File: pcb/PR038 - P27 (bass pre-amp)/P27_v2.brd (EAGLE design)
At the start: 45.1 x 52.1 mm, 52 parts, among them IC1 NE5532U, IC2 LM317, IC3 LM337, T1 BC549

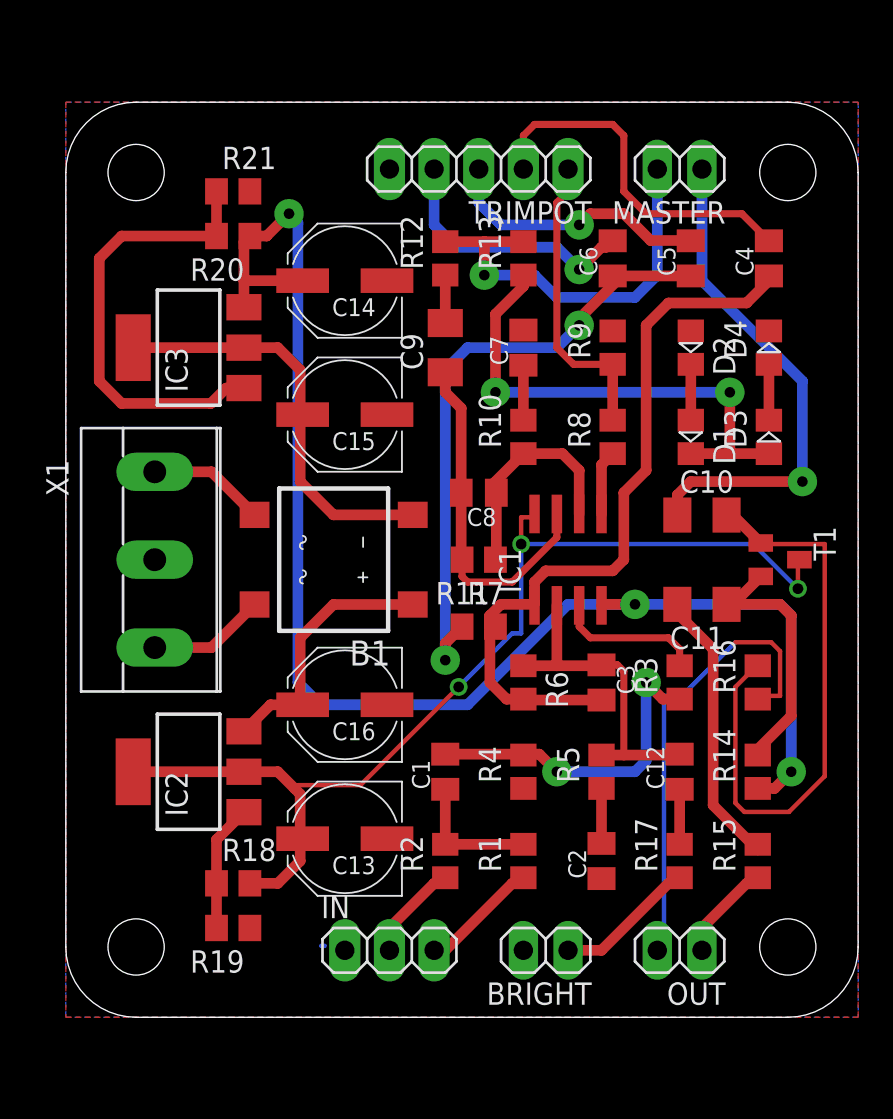
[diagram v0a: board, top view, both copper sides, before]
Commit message: 
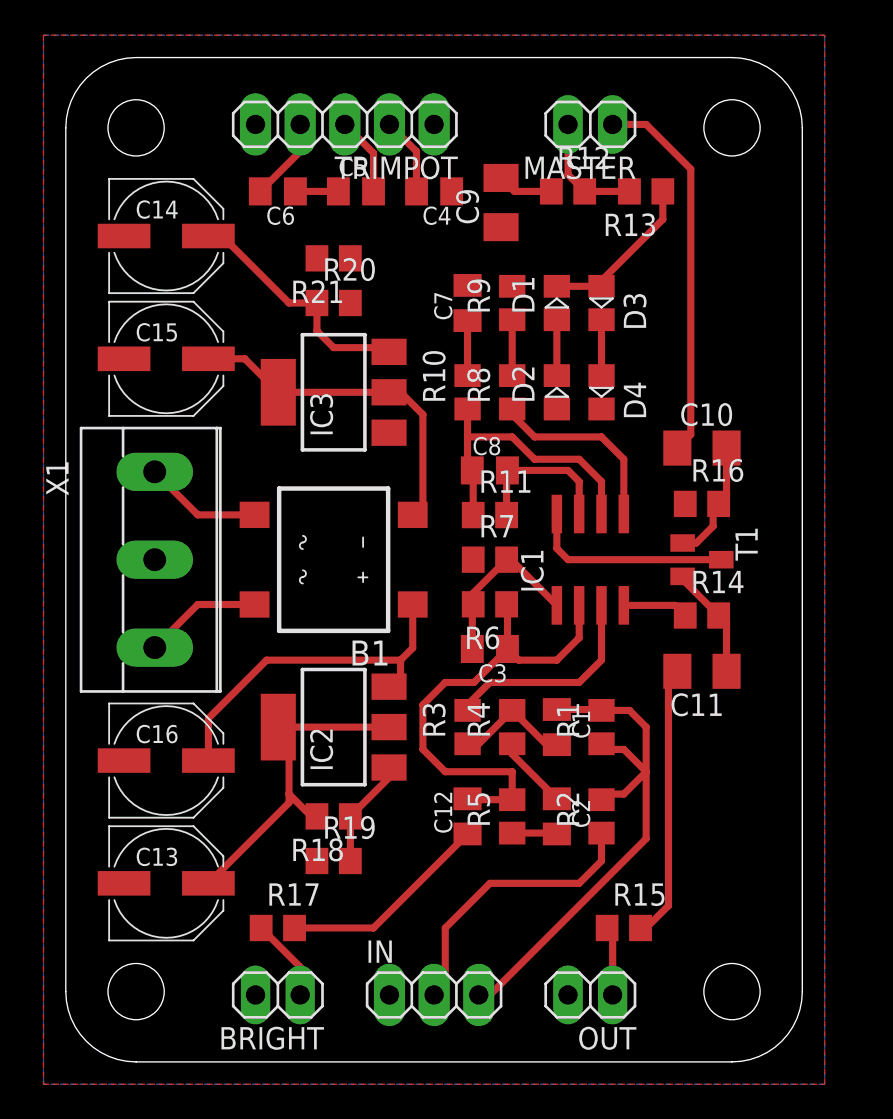
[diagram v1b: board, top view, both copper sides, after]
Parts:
- moved R17 23.2 mm to (12.1, 5.08), turned to 0 degrees
- moved C4 19.4 mm to (21.0, 47.0), turned to 180 degrees
- moved C5 19.4 mm to (16.5, 47.0), turned to 0 degrees
- moved C6 19.4 mm to (12.1, 47.0), turned to 180 degrees
- moved BRIGHT 15.5 mm to (12.1, 1.27)
- moved C12 12.3 mm to (22.9, 11.4)
- moved R3 12.3 mm to (22.9, 16.5)
- moved D3 12.2 mm to (30.5, 40.6), turned to 270 degrees
- moved D1 10.8 mm to (27.9, 40.6), turned to 90 degrees
- moved C15 10.6 mm to (5.71, 37.5), turned to 0 degrees
- moved C16 10.6 mm to (5.71, 14.6), turned to 0 degrees
- moved R16 10.6 mm to (36.2, 29.2), turned to 0 degrees
- moved C13 10.5 mm to (5.71, 7.62), turned to 0 degrees
- moved C14 10.5 mm to (5.71, 44.5), turned to 0 degrees
- moved D4 9.86 mm to (30.5, 35.6), turned to 270 degrees
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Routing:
- net -12V: track 81.8 -> 17.7 mm, vias 3 -> 0
- net N$8: track 36.5 -> 2.45 mm, vias 2 -> 0
- net N$6: track 42.9 -> 9.82 mm
- net +12V: track 60.3 -> 30.8 mm, vias 3 -> 0
- net N$11: track 34.0 -> 6.89 mm
- net N$38: track 25.8 -> 0.00 mm
- net AGND: track 26.8 -> 4.18 mm
- net N$24: track 29.0 -> 9.39 mm, vias 2 -> 0
- net N$21: track 23.3 -> 6.75 mm, vias 1 -> 0
- net N$10: track 20.7 -> 4.45 mm
- net N$13: track 17.2 -> 3.18 mm
- net N$25: track 6.79 -> 20.2 mm
- net N$3: track 19.4 -> 6.67 mm, vias 2 -> 0
- net N$18: track 20.4 -> 8.75 mm
- net N$9: track 15.4 -> 4.49 mm, vias 1 -> 0
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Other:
- board size 45.1 x 52.1 mm -> 41.9 x 57.1 mm

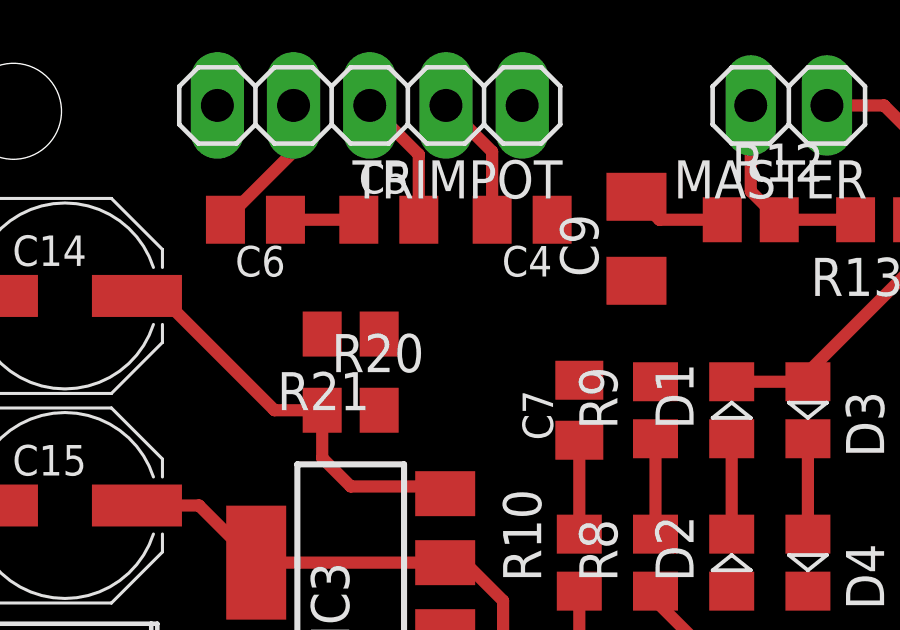
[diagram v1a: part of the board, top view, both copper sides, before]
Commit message: 
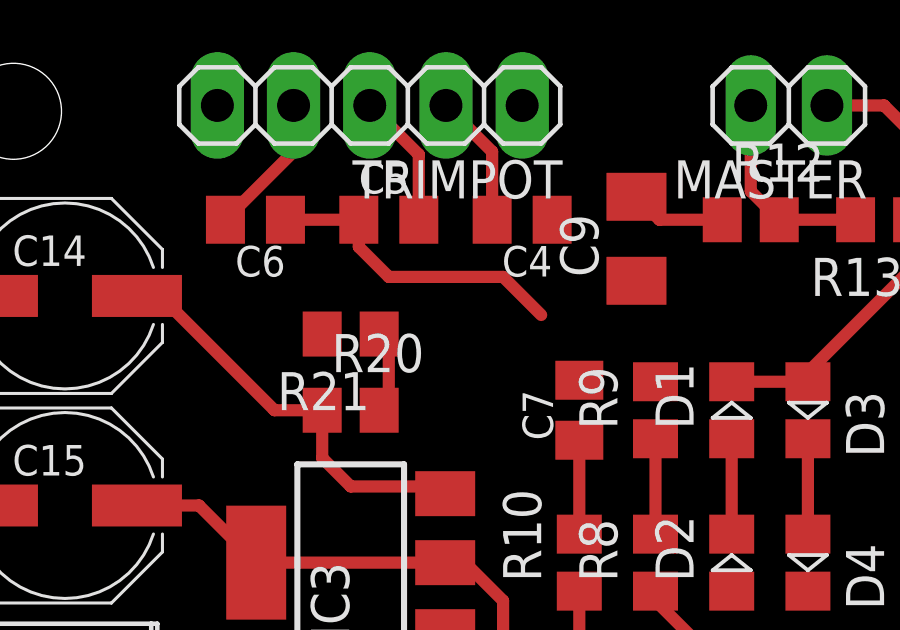
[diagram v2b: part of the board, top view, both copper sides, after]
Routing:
- net N$8: track 2.45 -> 10.4 mm
- net N$38: track 0.00 -> 3.18 mm
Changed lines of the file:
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@@
 <contactref element="C15" pad="-"/>
 <contactref element="C16" pad="-"/>
-<polygon width="0.4064" layer="1" orphans="yes">
+<polygon width="0.4064" layer="1" isolate="0.4064" orphans="yes">
 <vertex x="-1.27" y="55.88"/>
 <vertex x="-1.27" y="-3.81"/>
@@
 <vertex x="43.18" y="55.88"/>
 </polygon>
-<polygon width="0.4064" layer="16" orphans="yes">
+<polygon width="0.4064" layer="16" isolate="0.4064" orphans="yes">
 <vertex x="-1.27" y="-3.81"/>
 <vertex x="-1.27" y="55.88"/>
@@
 <wire x1="25.4" y1="15.56" x2="25.4" y2="14.97" width="0.4064" layer="1"/>
 <wire x1="25.4" y1="14.97" x2="27.94" y2="12.43" width="0.4064" layer="1"/>
+<wire x1="27.94" y1="34.61" x2="25.4" y2="41.59" width="0" layer="19" extent="1-1"/>
+<wire x1="27.94" y1="12.43" x2="28.575" y2="1.27" width="0" layer="19" extent="1-1"/>
 </signal>
 <signal name="N$5">
@@
 <contactref element="C6" pad="1"/>
 <wire x1="13.065" y1="46.99" x2="15.51" y2="46.99" width="0.4064" layer="1"/>
-<wire x1="23.18" y1="26.035" x2="15.51" y2="46.99" width="0" layer="19" extent="1-1"/>
+<wire x1="15.51" y1="46.99" x2="15.51" y2="46.085" width="0.4064" layer="1"/>
+<wire x1="15.51" y1="46.085" x2="16.51" y2="45.085" width="0.4064" layer="1"/>
+<wire x1="16.51" y1="45.085" x2="20.32" y2="45.085" width="0.4064" layer="1"/>
+<wire x1="20.32" y1="45.085" x2="21.59" y2="43.815" width="0.4064" layer="1"/>
+<wire x1="21.59" y1="43.815" x2="23.18" y2="26.035" width="0" layer="19" extent="1-16"/>
 </signal>
 <signal name="N$7">
@@
 <contactref element="IC3" pad="1"/>
 <contactref element="R21" pad="1"/>
-<wire x1="16.19" y1="40.64" x2="16.19" y2="43.18" width="0" layer="19" extent="1-1"/>
 <wire x1="18.39" y1="33.26" x2="16.19" y2="40.64" width="0" layer="19" extent="1-1"/>
+<wire x1="16.19" y1="40.64" x2="16.51" y2="40.64" width="0.4064" layer="1"/>
+<wire x1="16.51" y1="40.64" x2="16.51" y2="43.18" width="0.4064" layer="1"/>
+<wire x1="16.51" y1="43.18" x2="16.19" y2="43.18" width="0.4064" layer="1"/>
 </signal>
 </signals>
